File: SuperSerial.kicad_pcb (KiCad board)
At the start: 2 copper layers, 100 x 77.5 mm, 55 parts, among them J1 sequential, J2 Apple II Expansion Bus, J2Alt1 staggered, SW1-1 1, SW1-2 2, SW1-3 3, SW1-4 4, SW1-5 5, SW1-6 6, SW2-1 1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

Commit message: cleanup
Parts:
- moved C1 2.64 mm to (192.4, 128.9)
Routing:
- net /SERCLK2: track 63.1 -> 65.3 mm
- net /~{IRQ}: track 110.7 -> 109.0 mm
- net /SERCLK: track 76.0 -> 74.7 mm

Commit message: fab note C3,C4,C9 optional
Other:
- board text added: "C3, C4, C9: can be omitted if UA6 is 14C88"
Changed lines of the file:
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@@
     (effects (font (size 0.635 0.635) (thickness 0.127) bold) (justify left bottom))
+  )
+  (gr_text "C3, C4, C9:\ncan be omitted \nif UA6 is 14C88" (at 215.9 78.74) (layer "F.Fab")
+    (effects (font (size 1 1) (thickness 0.15)) (justify left bottom))
   )
   (gr_text "G1 / Y1&C1: one of:\nDIP-8 oscillator\nDIP-14 oscillator\nCrystal w/optional capacitor\n\nmake sure can doesn't short to unused pads" (at 215.9 130.175) (layer "F.Fab")

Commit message: tweak fab text
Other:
- board text added: "G1 / Y1 / C1: one of: DIP-8 oscillator DIP-14 oscillator Crystal w/tuning capacitor make sure metal can does not short to unused pads"
- board text added: "J1: header placed according to which cable is being used. apple sequential staggered 25pin 9pin 9pin -- --- --- --- 1 GND DCD DCD 2 TXD RXD DSR 3 RXD TXD RXD 4 RTS DTR RTS 5 CTS GND TXD 6 DSR DSR CTS 7 DCD RTS DTR 8 GND CTS NC 9 DTR NC GND 10 NC NC NC"
- board text removed: "G1 / Y1&C1: one of: DIP-8 oscillator DIP-14 oscillator Crystal w/optional capacitor make sure can doesn't short to unused pads"
- board text removed: "J1: one of: pin apple sequential staggered -- --- ------ ------ 1 GND DCD DCD 2 TXD RXD DSR 3 RXD TXD RXD 4 RTS DTR RTS 5 CTS GND TXD 6 DSR DSR CTS 7 DCD RTS DTR 8 GND CTS NC 9 DTR NC GND 10 NC NC NC"
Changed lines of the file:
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@@
     (effects (font (size 1 1) (thickness 0.15)) (justify left bottom))
   )
-  (gr_text "G1 / Y1&C1: one of:\nDIP-8 oscillator\nDIP-14 oscillator\nCrystal w/optional capacitor\n\nmake sure can doesn't short to unused pads" (at 215.9 130.175) (layer "F.Fab")
+  (gr_text "G1 / Y1 / C1: one of:\nDIP-8 oscillator\nDIP-14 oscillator\nCrystal w/tuning capacitor\n\nmake sure metal can does\nnot short to unused pads" (at 215.9 130.175) (layer "F.Fab")
     (effects (font (size 1 1) (thickness 0.15)) (justify left bottom))
   )
-  (gr_text "J1: one of:\npin	apple	sequential	staggered\n--	---		------		------\n1	GND		DCD			DCD\n2	TXD		RXD			DSR\n3	RXD		TXD			RXD\n4	RTS		DTR			RTS\n5	CTS		GND			TXD\n6	DSR		DSR			CTS\n7	DCD		RTS			DTR\n8	GND		CTS			NC\n9	DTR		NC			GND\n10	NC		NC			NC\n" (at 215.9 111.125) (layer "F.Fab")
+  (gr_text "J1: header placed according \nto which cable is being used.\n	apple  sequential staggered\n	25pin	9pin	9pin\n--	---		---		---\n1	GND		DCD		DCD\n2	TXD		RXD		DSR\n3	RXD		TXD		RXD\n4	RTS		DTR		RTS\n5	CTS		GND		TXD\n6	DSR		DSR		CTS\n7	DCD		RTS		DTR\n8	GND		CTS		NC\n9	DTR		NC		GND\n10	NC		NC		NC\n" (at 215.9 111.125) (layer "F.Fab")
     (effects (font (size 1 1) (thickness 0.15)) (justify left bottom))
   )

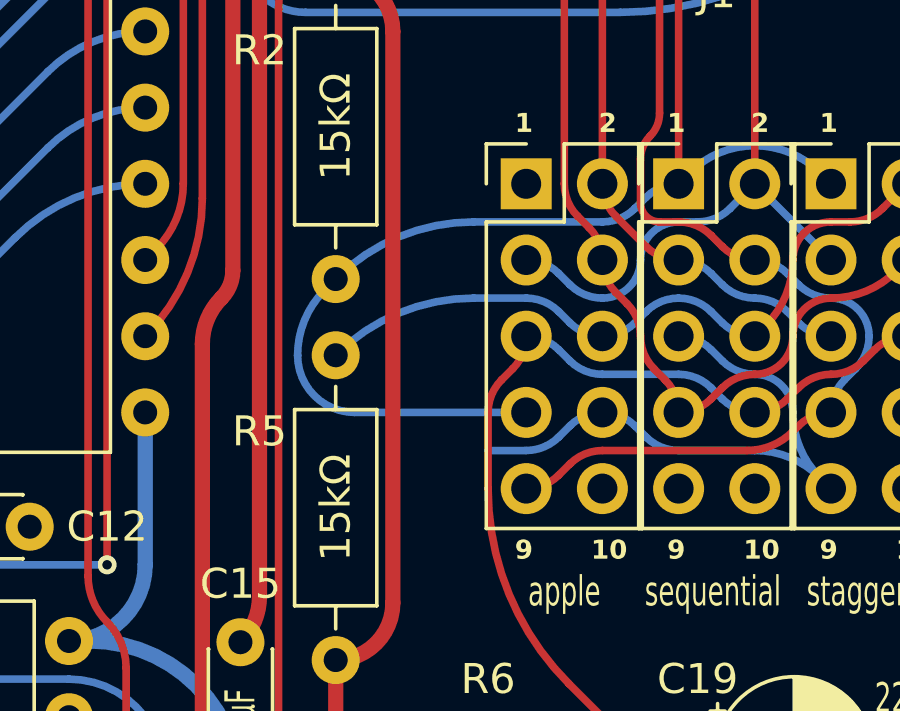
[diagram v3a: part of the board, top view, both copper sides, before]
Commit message: Move DCD to apple connector pin 10
Fixes #1
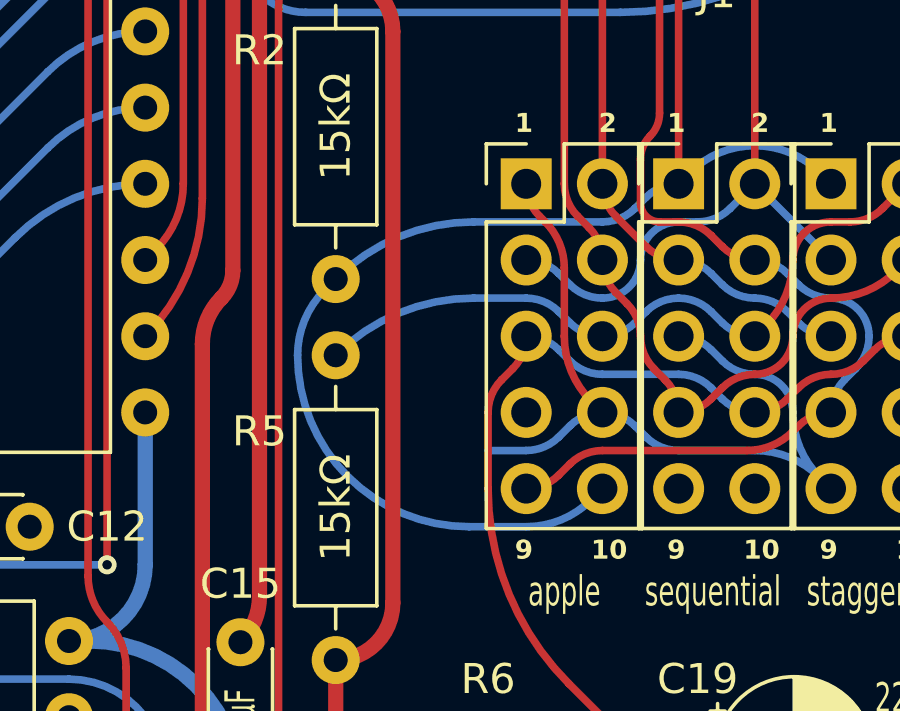
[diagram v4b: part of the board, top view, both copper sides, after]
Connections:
- JAlt1 pad 10: unconnected-(JAlt1-Pin_10-Pad10) -> /DCD
- JAlt1 pad 7: /DCD -> unconnected-(JAlt1-Pin_7-Pad7)
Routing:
- net GND: track 107.4 -> 115.8 mm
- net /DCD: track 48.1 -> 53.1 mm
